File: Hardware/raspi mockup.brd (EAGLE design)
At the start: 85 x 56 mm, 40 parts, among them J1 QWIIC, J2 AVR_SPI_PROG_3X2TESTPOINTS, U1 RASPBERRY_PI_40BTM-NOHOLES, U2 ADMP401, U3 ADMP401, U4 WM8960, U5 ATTINY84

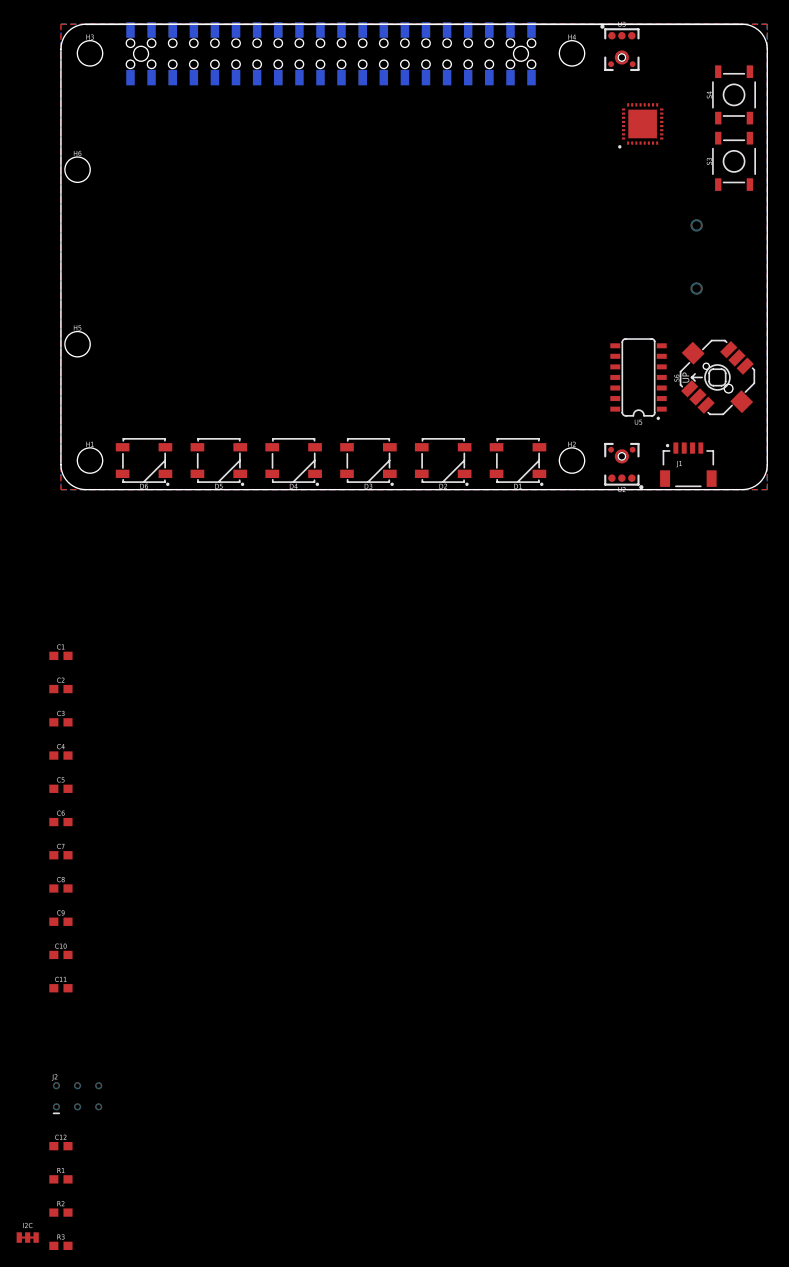
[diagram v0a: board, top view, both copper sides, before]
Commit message: adding in screen, ready for first design review
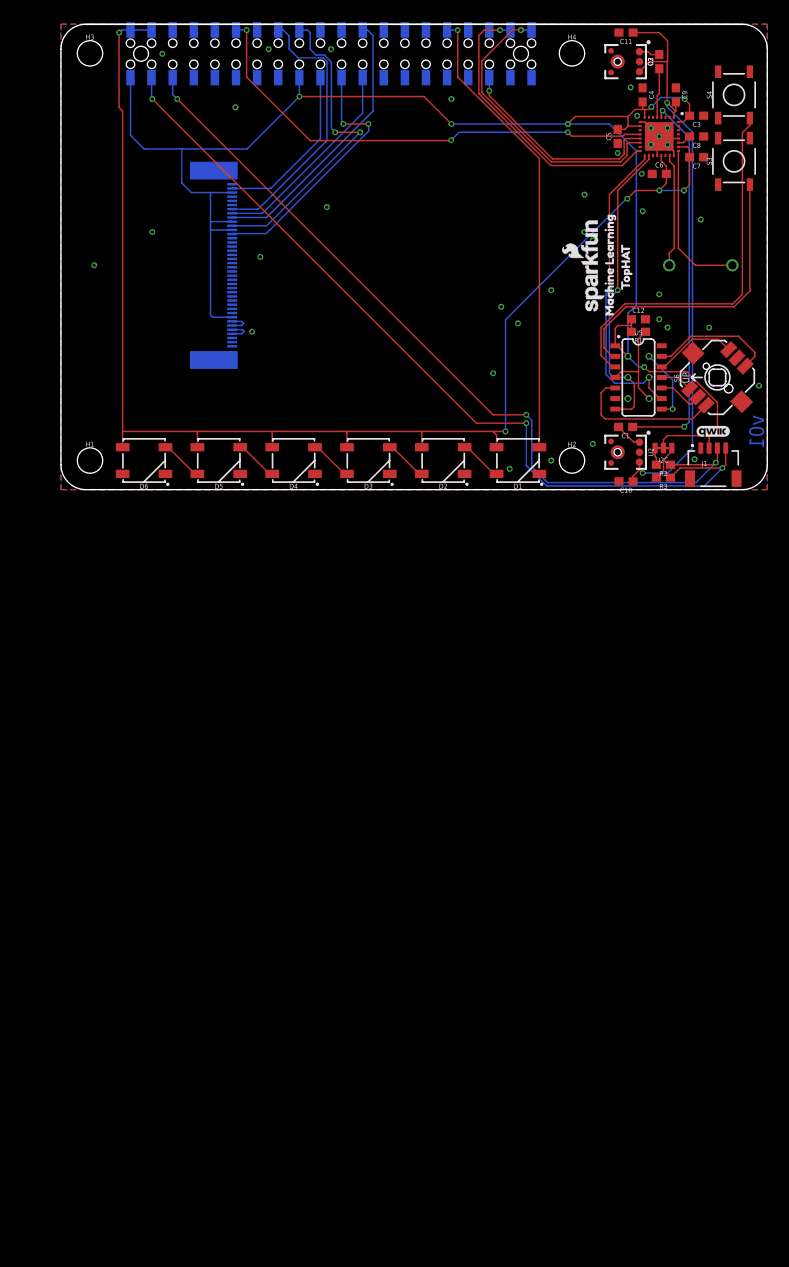
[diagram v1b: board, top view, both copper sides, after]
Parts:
- removed H5, H6: STAND-OFFTIGHT, SparkFun-Hardware:STAND-OFF-TIGHT
- removed LS1: SPEAKERCVS-1508, SparkFun-Electromechanical:CVS-1508_PCBSPKR
- added J3: 4DLCD-24-320X240, SparkFun-Displays:FPC05040-17204
- added LOGO1: SFE_LOGO_NAME_FLAME.1_INCH, SparkFun-Aesthetics:SFE_LOGO_NAME_FLAME_.1
- added LOGO2: SFE_LOGO_NAME_FLAME.4_INCH, SparkFun-Aesthetics:SFE_LOGO_NAME_FLAME_.4
- added LOGO3: QWIIC_LOGO_4MM, SparkFun-Aesthetics:QWIIC_4MM
- added LS2: CVS-1508, SparkFun-Electromechanical:CVS-1508_PCBSPKR
- added U$1: (no value), buzzard_labels (14):TOPHAT1
- added U$2: (no value), buzzard_labels (14):MACHINE_LEARNING0
- added U$3: (no value), buzzard_labels (13):MACHINE_LEARNING_TOPHAT0
- U1: value RASPBERRY_PI_40BTM-NOHOLES -> (none)
- moved C11 133.6 mm to (68.0, 55.0), turned to 180 degrees
- moved C9 124.0 mm to (74.0, 47.5), turned to 270 degrees
- moved R1 123.4 mm to (69.5, 19.0), turned to 180 degrees
- moved I2C 122.0 mm to (72.5, 5.00), turned to 180 degrees
- moved C12 121.4 mm to (69.5, 20.5)
- moved C8 118.5 mm to (76.5, 42.5), turned to 180 degrees
- moved R3 117.5 mm to (72.5, 1.45), turned to 180 degrees
- moved R2 115.6 mm to (72.5, 3.00), turned to 180 degrees
- moved C7 113.6 mm to (76.5, 40.0), turned to 180 degrees
- moved J2 109.7 mm to (69.5, 13.5), flipped to the bottom, turned to 270 degrees
- moved C6 106.2 mm to (72.0, 38.0)
- moved C4 105.9 mm to (70.0, 47.5), turned to 270 degrees
- moved C3 105.7 mm to (76.5, 45.0), turned to 180 degrees
- moved C2 104.3 mm to (72.0, 51.5), turned to 90 degrees
- moved C5 103.2 mm to (67.0, 42.5), turned to 90 degrees
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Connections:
- new net !RESET: J3.34, U1.16
- new net CS: J3.32, U1.24
- new net D/C: J3.30, U1.18
- new net SCK: J3.33, U1.23
- new net SDI: J3.39, U1.19
- new net SDO: J3.28, U1.21
- net 3.3V: now also J3.29, J3.31, J3.38, J3.8
- net BTN_CENTER: now also U5.10; no longer U5.8
- net BTN_DOWN: now also U5.13; no longer U5.12
- net BTN_LEFT: now also U5.5; no longer U5.11
- net BTN_RIGHT: now also U5.12; no longer U5.10
- net BTN_UP: now also U5.11; no longer U5.13
- net GND: now also J3.1, J3.11, J3.12, J3.13, J3.14, J3.15, J3.16, J3.17, J3.18, J3.19, J3.20, J3.21, J3.22, J3.23, J3.24, J3.25, J3.26, J3.27, J3.4, J3.40, J3.5, J3.6, J3.7
- net MISO: now also U5.8
- net N$22: now also LS2.-; no longer LS1.-
- net N$6: now also LS2.+; no longer LS1.+
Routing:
- net 3.3V: track 0.00 -> 193.8 mm, vias 0 -> 6
- net 5V: track 0.00 -> 162.8 mm, vias 0 -> 5
- net N$32: track 0.00 -> 103.7 mm, vias 0 -> 3
- net N$31: track 0.00 -> 98.4 mm, vias 0 -> 3
- net MICBIAS: track 0.00 -> 72.5 mm, vias 0 -> 2
- net BCLK: track 0.00 -> 58.2 mm, vias 0 -> 3
- net LED_DATA: track 0.00 -> 55.6 mm, vias 0 -> 1
- net N$29: track 0.00 -> 46.7 mm, vias 0 -> 2
- net BTN_B: track 0.00 -> 45.9 mm
- net D/C: track 0.00 -> 38.3 mm, vias 0 -> 2
- net SCL: track 0.00 -> 37.5 mm, vias 0 -> 1
- net SDA: track 0.00 -> 36.9 mm, vias 0 -> 1
- net BTN_A: track 0.00 -> 36.3 mm
- net DAC-DAT: track 0.00 -> 35.6 mm, vias 0 -> 1
- net ADC-DAT: track 0.00 -> 34.8 mm, vias 0 -> 1
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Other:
- board text added: "Andy England"
- board text added: "v01"

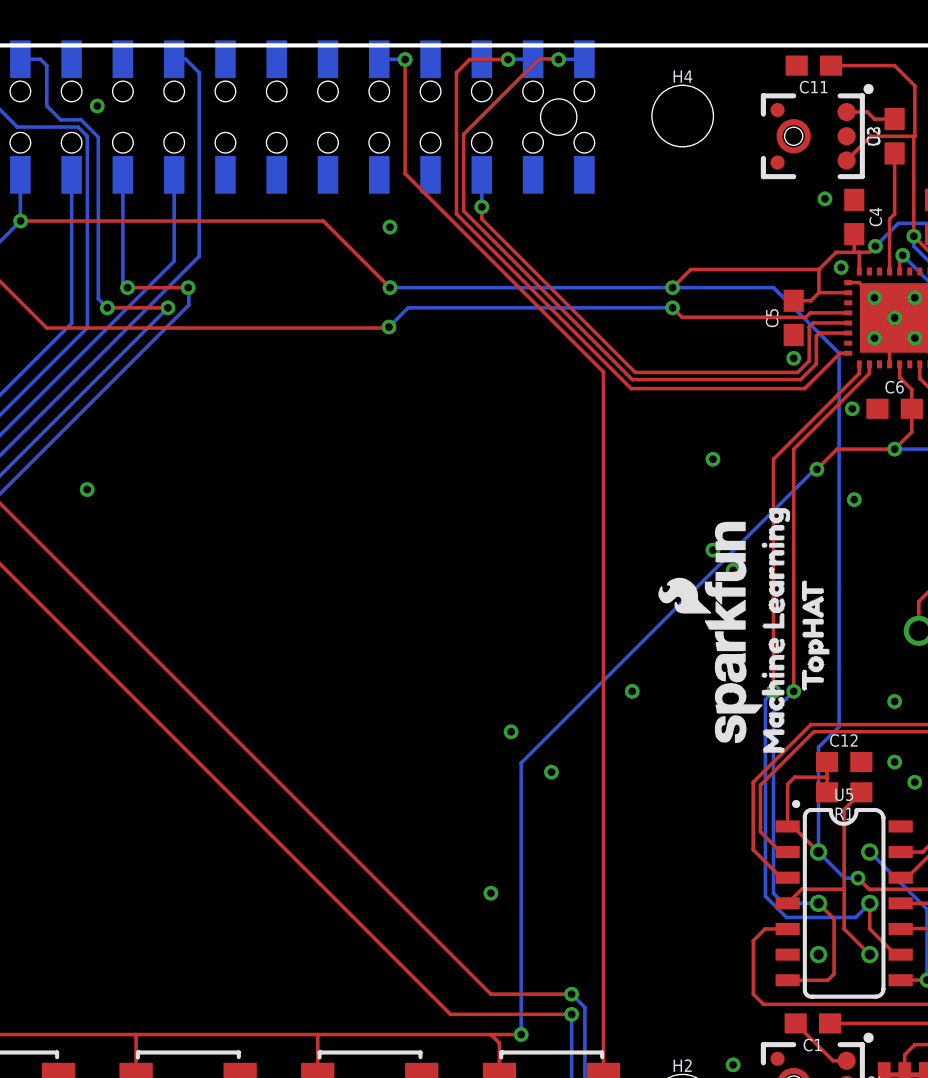
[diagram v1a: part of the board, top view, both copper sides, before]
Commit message: updating int pin
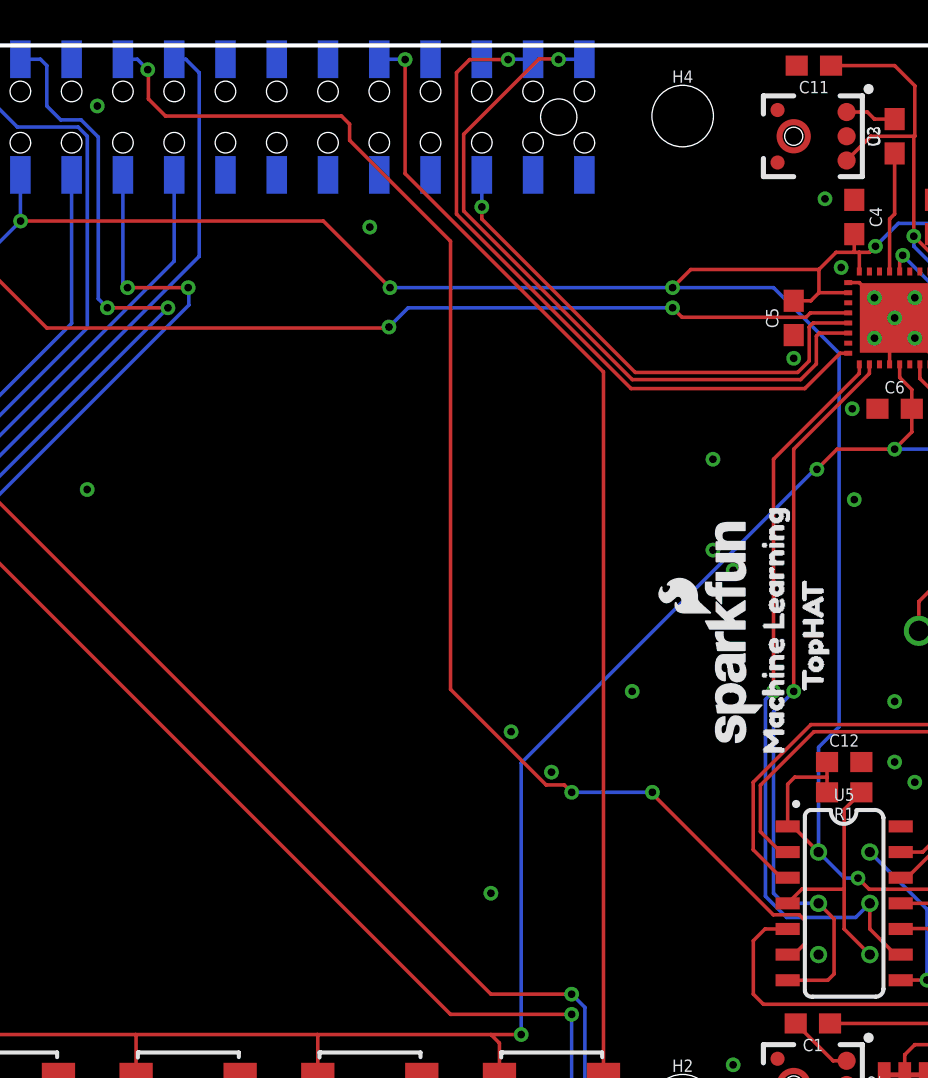
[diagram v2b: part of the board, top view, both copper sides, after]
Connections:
- net INT: now also U1.22
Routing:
- net INT: track 0.00 -> 68.0 mm, vias 0 -> 3
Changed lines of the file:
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@@
 <via x="24" y="28" extent="1-16" drill="0.381"/>
 <via x="32" y="34" extent="1-16" drill="0.381"/>
-<via x="47" y="47" extent="1-16" drill="0.381"/>
+<via x="46" y="47" extent="1-16" drill="0.381"/>
 <via x="55" y="20" extent="1-16" drill="0.381"/>
 <via x="59" y="24" extent="1-16" drill="0.381"/>
@@
 <signal name="INT">
 <contactref element="U5" pad="6"/>
+<contactref element="U1" pad="22"/>
+<wire x1="66.7" y1="10.96" x2="67.01" y2="10.96" width="0.1778" layer="1"/>
+<wire x1="67.5667" y1="11.5167" x2="67.5667" y2="12.64046875" width="0.1778" layer="1"/>
+<wire x1="67.5667" y1="12.64046875" x2="67.27386875" y2="12.9333" width="0.1778" layer="1"/>
+<wire x1="67.27386875" y1="12.9333" x2="65.98953125" y2="12.9333" width="0.1778" layer="1"/>
+<wire x1="67.01" y1="10.96" x2="67.5667" y2="11.5167" width="0.1778" layer="1"/>
+<wire x1="60" y1="18.92283125" x2="60" y2="19" width="0.1778" layer="1"/>
+<via x="60" y="19" extent="1-16" drill="0.381"/>
+<wire x1="60" y1="19" x2="56" y2="19" width="0.1778" layer="16"/>
+<via x="56" y="19" extent="1-16" drill="0.381"/>
+<wire x1="56" y1="19" x2="55.635" y2="19.365" width="0.1778" layer="1"/>
+<wire x1="55.635" y1="19.365" x2="54.73696875" y2="19.365" width="0.1778" layer="1"/>
+<wire x1="54.73696875" y1="19.365" x2="50" y2="24.10196875" width="0.1778" layer="1"/>
+<wire x1="65.98953125" y1="12.9333" x2="60" y2="18.92283125" width="0.1778" layer="1"/>
+<wire x1="50" y1="46.3" x2="45" y2="51.3" width="0.1778" layer="1"/>
+<wire x1="45" y1="51.3" x2="45" y2="52.1" width="0.1778" layer="1"/>
+<wire x1="45" y1="52.1" x2="44.6" y2="52.5" width="0.1778" layer="1"/>
+<via x="35" y="54.8" extent="1-16" drill="0.381"/>
+<wire x1="35.0333" y1="54.7667" x2="35" y2="54.8" width="0.1778" layer="1"/>
+<wire x1="35.0333" y1="53.348275" x2="35.0333" y2="54.7667" width="0.1778" layer="1"/>
+<wire x1="35.881575" y1="52.5" x2="35.0333" y2="53.348275" width="0.1778" layer="1"/>
+<wire x1="35" y1="54.8" x2="34.485" y2="55.315" width="0.1778" layer="16"/>
+<wire x1="34.485" y1="55.315" x2="33.77" y2="55.315" width="0.1778" layer="16"/>
+<wire x1="50" y1="24.10196875" x2="50" y2="46.3" width="0.1778" layer="1"/>
+<wire x1="44.6" y1="52.5" x2="35.881575" y2="52.5" width="0.1778" layer="1"/>
 </signal>
 <signal name="N$16">
